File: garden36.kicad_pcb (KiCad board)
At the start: 2 copper layers, 231.5 x 91.8 mm, 86 parts, among them SW1 SW_SPDT, SW2 SW_Push, SW3 SW_SPDT, SW4 SW_Push, U1 nice_nano, U2 nice_nano

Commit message: Mounting holes for left added
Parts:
- removed the REF** at (140.8, 99.3)
- removed the REF** at (135.8, 99.3)
- added H10: MountingHole_2.2mm_M2, MountingHole:MountingHole_2.2mm_M2, F.Cu at (129.5, 105.9)
- added H4: MountingHole_2.2mm_M2, MountingHole:MountingHole_2.2mm_M2, F.Cu at (37.5, 69.2)
- added H5: MountingHole_2.2mm_M2, MountingHole:MountingHole_2.2mm_M2, F.Cu at (113.7, 63.3)
- added H6: MountingHole_2.2mm_M2, MountingHole:MountingHole_2.2mm_M2, F.Cu at (43.9, 126.0)
- added H7: MountingHole_2.2mm_M2, MountingHole:MountingHole_2.2mm_M2, F.Cu at (71.6, 106.7)
- added H8: MountingHole_2.2mm_M2, MountingHole:MountingHole_2.2mm_M2, F.Cu at (119.3, 132.2)
- added H9: MountingHole_2.2mm_M2, MountingHole:MountingHole_2.2mm_M2, F.Cu at (122.4, 105.9)
- added REF**: mousebites 2mm, PCM_marbastlib-various:mousebites_2mm, F.Cu at (138.7, 106.3)
- moved SW2 3.00 mm to (99.4, 61.8)
- moved SW4 3.00 mm to (177.1, 61.8), turned to 90 degrees
- moved PW1 2.00 mm to (125.8, 99.8)
- moved PW4 2.00 mm to (150.7, 99.8)
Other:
- outline, holes or cut-outs redrawn

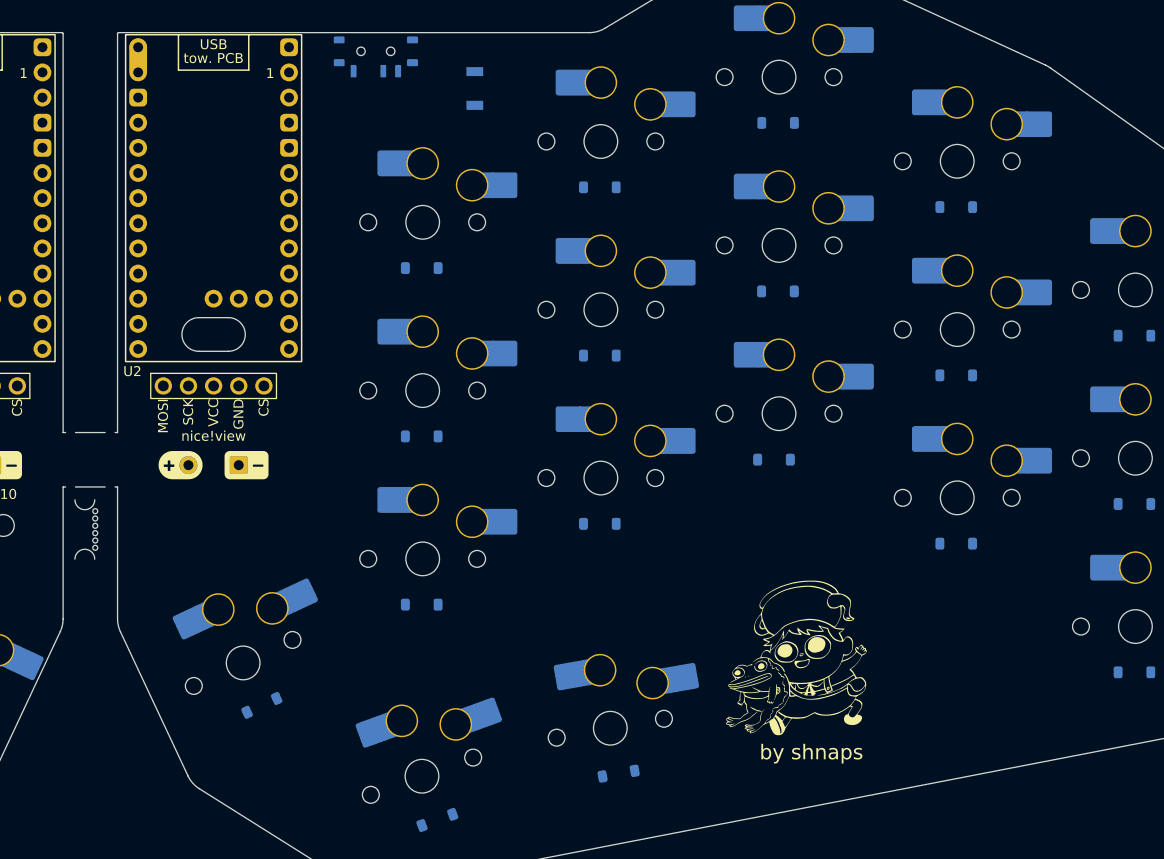
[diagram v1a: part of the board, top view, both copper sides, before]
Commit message: Add mousebites symbol
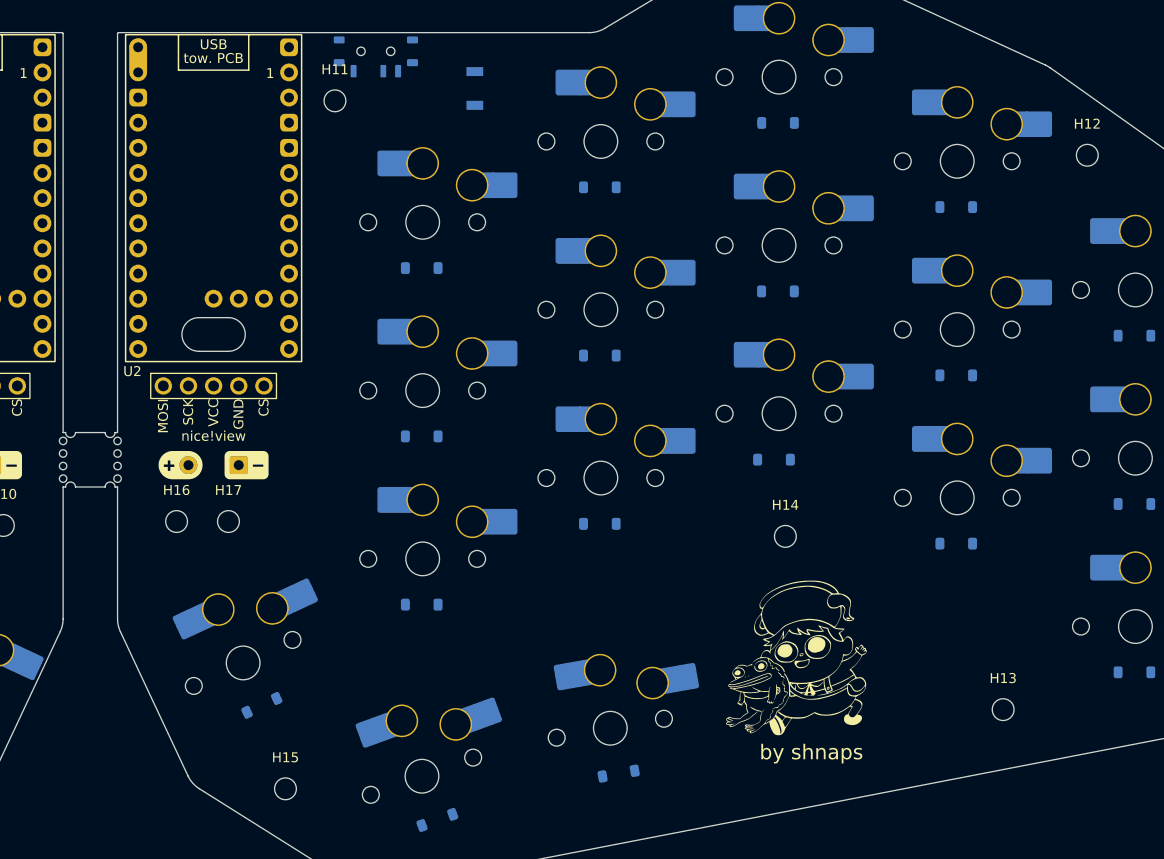
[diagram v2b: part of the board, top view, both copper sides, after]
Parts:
- removed REF**: mousebites 2mm, PCM_marbastlib-various:mousebites_2mm
- added H11: MountingHole, MountingHole:MountingHole_2.2mm_M2, F.Cu at (163.0, 63.0)
- added H12: MountingHole, MountingHole:MountingHole_2.2mm_M2, F.Cu at (239.0, 68.5)
- added H13: MountingHole, MountingHole:MountingHole_2.2mm_M2, F.Cu at (230.5, 124.5)
- added H14: MountingHole, MountingHole:MountingHole_2.2mm_M2, F.Cu at (208.5, 107.0)
- added H15: MountingHole, MountingHole:MountingHole_2.2mm_M2, F.Cu at (158.0, 132.5)
- added H16: MountingHole, MountingHole:MountingHole_2.2mm_M2, F.Cu at (147.0, 105.5)
- added H17: MountingHole, MountingHole:MountingHole_2.2mm_M2, F.Cu at (152.2, 105.5)
- added MB4: ~, PCM_marbastlib-various:mousebites_1mm, F.Cu at (140.8, 99.3)
- added MB5: ~, PCM_marbastlib-various:mousebites_1mm, F.Cu at (135.8, 99.3)
- H10, H4, H5, H6, H7, H8, H9: value MountingHole_2.2mm_M2 -> MountingHole

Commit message: Positioning done
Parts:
- moved H14 3.81 mm to (204.9, 108.1)
- moved H13 2.46 mm to (232.3, 126.1)
- moved by shnaps 1.98 mm to (211.0, 120.8)
- moved H17 1.97 mm to (154.2, 105.9)
- moved H7 1.41 mm to (71.7, 108.1)
- moved H15 0.78 mm to (157.4, 132.0)
- moved H12 0.70 mm to (239.0, 69.2)
- moved D31 0.41 mm to (207.8, 99.2)
- moved H16 0.41 mm to (147.1, 105.9)
- moved H6 0.36 mm to (44.2, 126.1)
- moved H11 0.33 mm to (162.9, 63.3)
- moved H8 0.18 mm to (119.2, 132.0)
- moved D34 0.13 mm to (155.6, 123.9)
- moved garden36 0.12 mm to (63.2, 119.3)
- moved D35 0.10 mm to (173.3, 135.5)
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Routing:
- net Net-(D6-A): track 0.00 -> 11.2 mm
- net Net-(D11-A): track 0.00 -> 11.2 mm
- net Net-(D1-A): track 0.00 -> 11.2 mm

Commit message: Start adding routes
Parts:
- moved MB4 5.00 mm to (135.8, 99.3), turned to 180 degrees
- moved MB5 5.00 mm to (140.8, 99.3), turned to 0 degrees
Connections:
- U1 pad 18: unconnected-(U1-P0.29-LF-Pad18) -> COL2
- U1 pad 19: unconnected-(U1-P0.02-LF-Pad19) -> COL3
- U1 pad 20: unconnected-(U1-P1.15-LF-Pad20) -> COL4
- U1 pad 21: unconnected-(U1-P1.13-LF-Pad21) -> ROW0
- U1 pad 22: unconnected-(U1-P1.11-LF-Pad22) -> ROW1
- U1 pad 23: unconnected-(U1-P0.10-LF-Pad23) -> ROW2
- U1 pad 24: unconnected-(U1-P0.09-LF-Pad24) -> ROW3
- U1 pad 7: unconnected-(U1-P0.22-Pad7) -> COL0
- U1 pad 8: unconnected-(U1-P0.24-Pad8) -> COL1
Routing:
- net ROW1: track 0.00 -> 133.0 mm, vias 0 -> 5
- net COL3: track 0.00 -> 124.1 mm
- net ROW0: track 0.00 -> 112.7 mm, vias 0 -> 5
- net ROW2: track 0.00 -> 110.7 mm, vias 0 -> 4
- net COL2: track 0.00 -> 108.5 mm
- net COL4: track 0.00 -> 99.7 mm, vias 0 -> 1
- net R_GND: track 0.00 -> 85.0 mm
- net R_COL2: track 0.00 -> 71.8 mm
- net R_COL1: track 0.00 -> 69.7 mm
- net R_COL0: track 0.00 -> 59.8 mm
- net ROW3: track 0.00 -> 51.8 mm, vias 0 -> 3
- net R_COL4: track 0.00 -> 34.0 mm
- net R_COL3: track 0.00 -> 34.0 mm
- net COL1: track 0.00 -> 34.0 mm
- net COL0: track 0.00 -> 34.0 mm
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
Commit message: Start connecting to MCU
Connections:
- U1 pad 18: COL2 -> unconnected-(U1-P0.29-LF-Pad18)
- U1 pad 19: COL3 -> unconnected-(U1-P0.02-LF-Pad19)
- U1 pad 20: COL4 -> unconnected-(U1-P1.15-LF-Pad20)
- U1 pad 21: ROW0 -> unconnected-(U1-P1.13-LF-Pad21)
- U1 pad 22: ROW1 -> unconnected-(U1-P1.11-LF-Pad22)
- U1 pad 23: ROW2 -> unconnected-(U1-P0.10-LF-Pad23)
- U1 pad 24: ROW3 -> unconnected-(U1-P0.09-LF-Pad24)
- U1 pad 7: COL0 -> unconnected-(U1-P0.22-Pad7)
- U1 pad 8: COL1 -> unconnected-(U1-P0.24-Pad8)
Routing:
- net R_GND: track 85.0 -> 0.00 mm
- net COL3: track 124.1 -> 75.0 mm
- net ROW3: track 51.8 -> 93.7 mm
- net COL4: track 99.7 -> 59.9 mm, vias 1 -> 0
- net COL2: track 108.5 -> 74.5 mm
- net R_RAW: track 27.6 -> 0.00 mm
- net GND: track 26.0 -> 0.00 mm
- net RST: track 19.5 -> 0.00 mm
- net ROW1: track 133.0 -> 113.8 mm
- net ROW2: track 110.7 -> 127.8 mm, vias 4 -> 5
- net Net-(D11-A): track 22.4 -> 11.2 mm
- net Net-(D6-A): track 22.4 -> 11.2 mm
- net RAW: track 6.57 -> 0.00 mm
- net ROW0: track 112.7 -> 107.3 mm
- net R_COL2: track 71.8 -> 73.6 mm
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
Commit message: Finish design
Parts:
- renumbered PW4 to PW2
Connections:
- U1 pad 17: unconnected-(U1-P0.31-LF-Pad17) -> COL1
- U1 pad 18: unconnected-(U1-P0.29-LF-Pad18) -> COL2
- U1 pad 19: unconnected-(U1-P0.02-LF-Pad19) -> COL3
- U1 pad 2: unconnected-(U1-P0.08-Pad2) -> COL0
- U1 pad 20: unconnected-(U1-P1.15-LF-Pad20) -> COL4
- U1 pad 21: unconnected-(U1-P1.13-LF-Pad21) -> ROW0
- U1 pad 22: unconnected-(U1-P1.11-LF-Pad22) -> ROW1
- U1 pad 23: unconnected-(U1-P0.10-LF-Pad23) -> ROW2
- U1 pad 24: unconnected-(U1-P0.09-LF-Pad24) -> ROW3
- U1 pad 29: unconnected-(U1-BAT+-Pad29) -> RAW
- U2 pad 10: unconnected-(U2-P0.11-Pad10) -> R_ROW1
- U2 pad 11: unconnected-(U2-P1.04-LF-Pad11) -> R_ROW2
- U2 pad 12: unconnected-(U2-P1.06-LF-Pad12) -> R_ROW3
- U2 pad 17: unconnected-(U2-P0.31-LF-Pad17) -> R_COL4
- U2 pad 18: unconnected-(U2-P0.29-LF-Pad18) -> R_COL3
- U2 pad 19: unconnected-(U2-P0.02-LF-Pad19) -> R_COL2
- U2 pad 29: unconnected-(U2-BAT+-Pad29) -> R_RAW
- U2 pad 7: unconnected-(U2-P0.22-Pad7) -> R_COL1
- U2 pad 8: unconnected-(U2-P0.24-Pad8) -> R_COL0
- U2 pad 9: unconnected-(U2-P1.00-Pad9) -> R_ROW0
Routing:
- net R_ROW2: track 0.00 -> 141.0 mm, vias 0 -> 5
- net R_COL4: track 34.0 -> 153.5 mm
- net R_ROW1: track 0.00 -> 116.5 mm, vias 0 -> 5
- net R_ROW0: track 0.00 -> 114.2 mm, vias 0 -> 5
- net COL0: track 34.0 -> 138.7 mm, vias 0 -> 1
- net R_COL3: track 34.0 -> 128.1 mm, vias 0 -> 1
- net R_ROW3: track 0.00 -> 92.7 mm, vias 0 -> 3
- net R_COL2: track 73.6 -> 154.4 mm, vias 0 -> 1
- net GND: track 0.00 -> 73.9 mm, vias 0 -> 2
- net R_GND: track 0.00 -> 73.9 mm, vias 0 -> 1
- net COL1: track 34.0 -> 101.1 mm, vias 0 -> 1
- net Net-(PW2-BAT+): track 0.00 -> 55.6 mm, vias 0 -> 1
- net Net-(PW1-BAT+): track 0.00 -> 48.0 mm
- net R_COL1: track 69.7 -> 116.5 mm, vias 0 -> 1
- net COL2: track 74.5 -> 120.9 mm, vias 0 -> 1
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- added copper zone on B.Cu, net (none)
- added copper zone on F.Cu, net (none)

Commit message: V2 ordered
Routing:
- net ROW3: track 94.2 -> 93.0 mm
- net RST: track 19.5 -> 20.6 mm
- net GND: track 73.9 -> 74.9 mm
- net ROW2: track 127.8 -> 128.5 mm
